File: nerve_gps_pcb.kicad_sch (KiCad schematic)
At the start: 14 parts, among them J1 2x8, J2 WS2812B, J3 5V GPIO Breakout, U1 SAM-M10Q, U2 TXB0104QPWRQ1

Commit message: Fix board-to-board connector pinout
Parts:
- removed J1: 2x8, Connector_PinHeader_1.27mm:PinHeader_2x08_P1.27mm_Vertical_SMD, symbol Connector_Generic:Conn_02x08_Counter_Clockwise
- added J1: 2x8, Connector_PinHeader_1.27mm:PinHeader_2x08_P1.27mm_Vertical_SMD, symbol Connector_Generic:Conn_02x08_Odd_Even
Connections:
- net +3.3VBATT: now also J1.14 (Pin_14)
- net +3V3: now also J1.3 (Pin_3), J1.4 (Pin_4)
- net +5V: now also J1.1 (Pin_1), J1.2 (Pin_2)
- net GND: now also J1.10 (Pin_10), J1.11 (Pin_11)
- net GPIO_1: now also J1.5 (Pin_5)
- net GPIO_2: now also J1.7 (Pin_7)
- net GPIO_3: now also J1.9 (Pin_9)
- net GPS_NRST: now also J1.12 (Pin_12)
- net GPS_UART_RX: now also J1.8 (Pin_8)
- net GPS_UART_TX: now also J1.6 (Pin_6)
- net LED_PWM: now also J1.13 (Pin_13)
- new net: J1.15 (Pin_15), J1.16 (Pin_16)

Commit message: Pass DRC (ERC previously passed)
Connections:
- net GPIO_1: now also J1.9 (Pin_9); no longer J1.5 (Pin_5)
- net GPIO_3: now also J1.5 (Pin_5); no longer J1.9 (Pin_9)
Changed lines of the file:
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@@
+		)
+	)
+	(hierarchical_label "GPIO_2"
+		(shape input)
+		(at 38.1 33.02 180)
+		(fields_autoplaced yes)
+		(effects
+			(font
+				(size 1.27 1.27)
+			)
+			(justify right)
 		)
 	)
@@
 		)
 	)
-	(hierarchical_label "GPIO_2"
+	(hierarchical_label "GPIO_1"
 		(shape input)
-		(at 38.1 33.02 180)
+		(at 38.1 35.56 180)
 		(fields_autoplaced yes)
 		(effects
@@
 		)
 	)
-	(hierarchical_label "GPIO_1"
+	(hierarchical_label "GPIO_2"
 		(shape input)
-		(at 38.1 30.48 180)
+		(at 34.29 99.06 180)
 		(fields_autoplaced yes)
 		(effects
@@
 		)
 	)
-	(hierarchical_label "GPIO_2"
+	(hierarchical_label "GPIO_3"
 		(shape input)
-		(at 34.29 99.06 180)
+		(at 38.1 30.48 180)
 		(fields_autoplaced yes)
 		(effects
@@
 		(fields_autoplaced yes)
 		(effects
-			(font
-				(size 1.27 1.27)
-			)
-			(justify right)
-		)
-	)
-	(hierarchical_label "GPIO_3"
-		(shape input)
-		(at 38.1 35.56 180)
-		(fields_autoplaced yes)
-		(effects

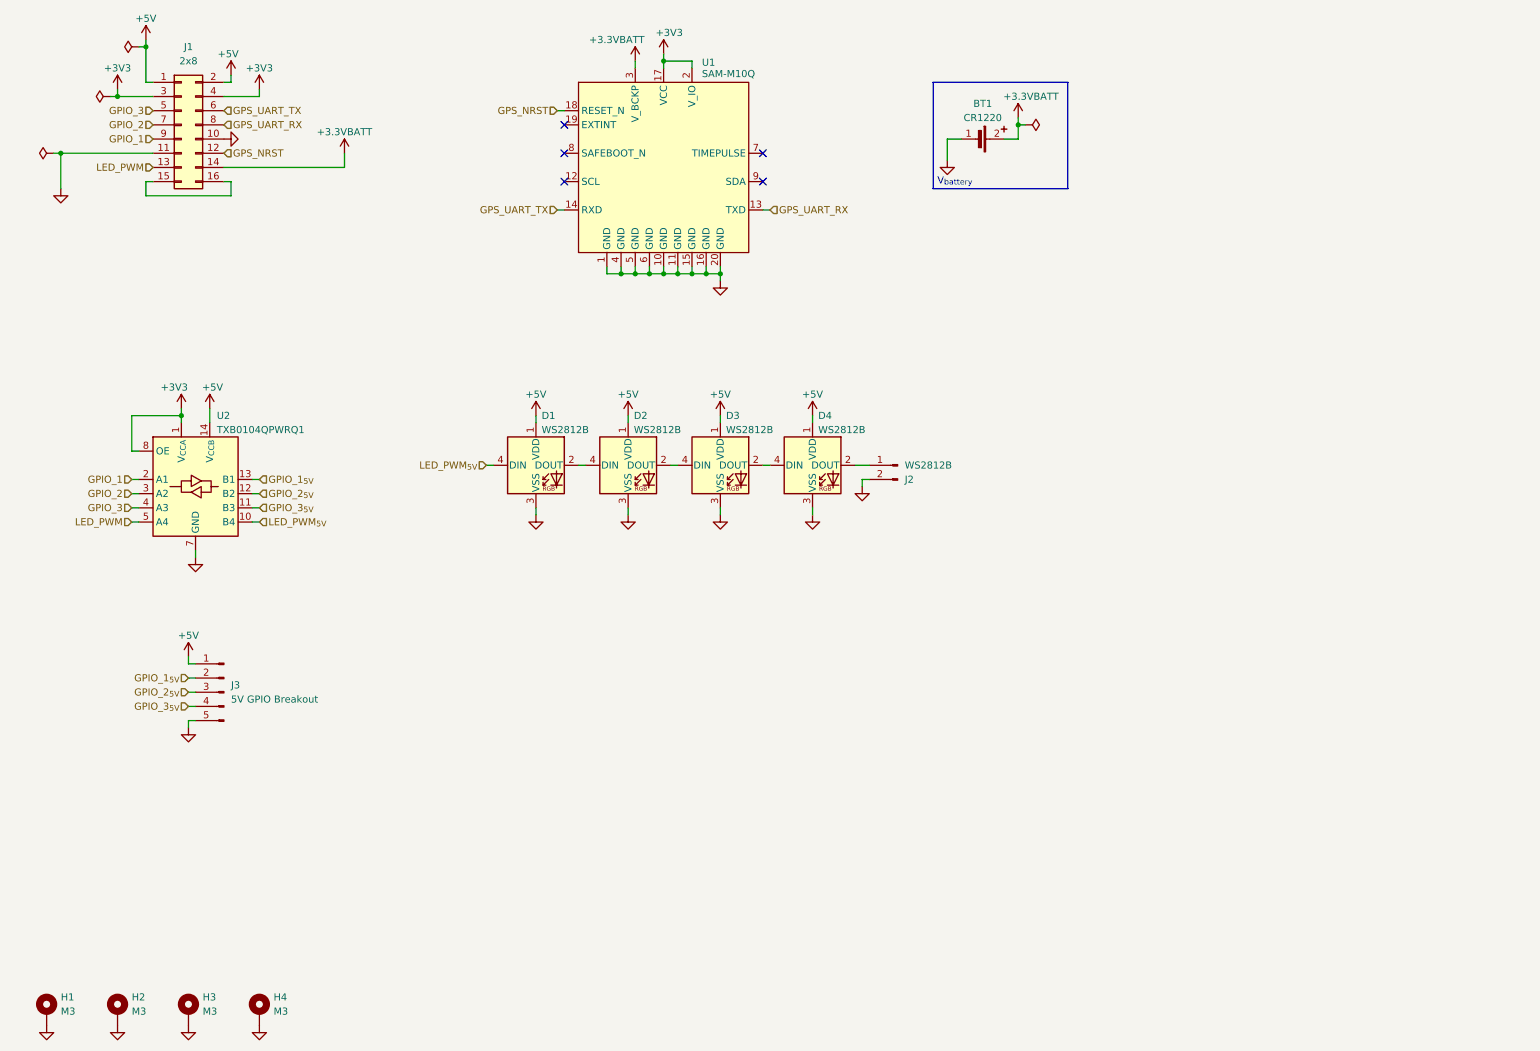
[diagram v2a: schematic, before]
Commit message: Cleanup and update board-to-board connector
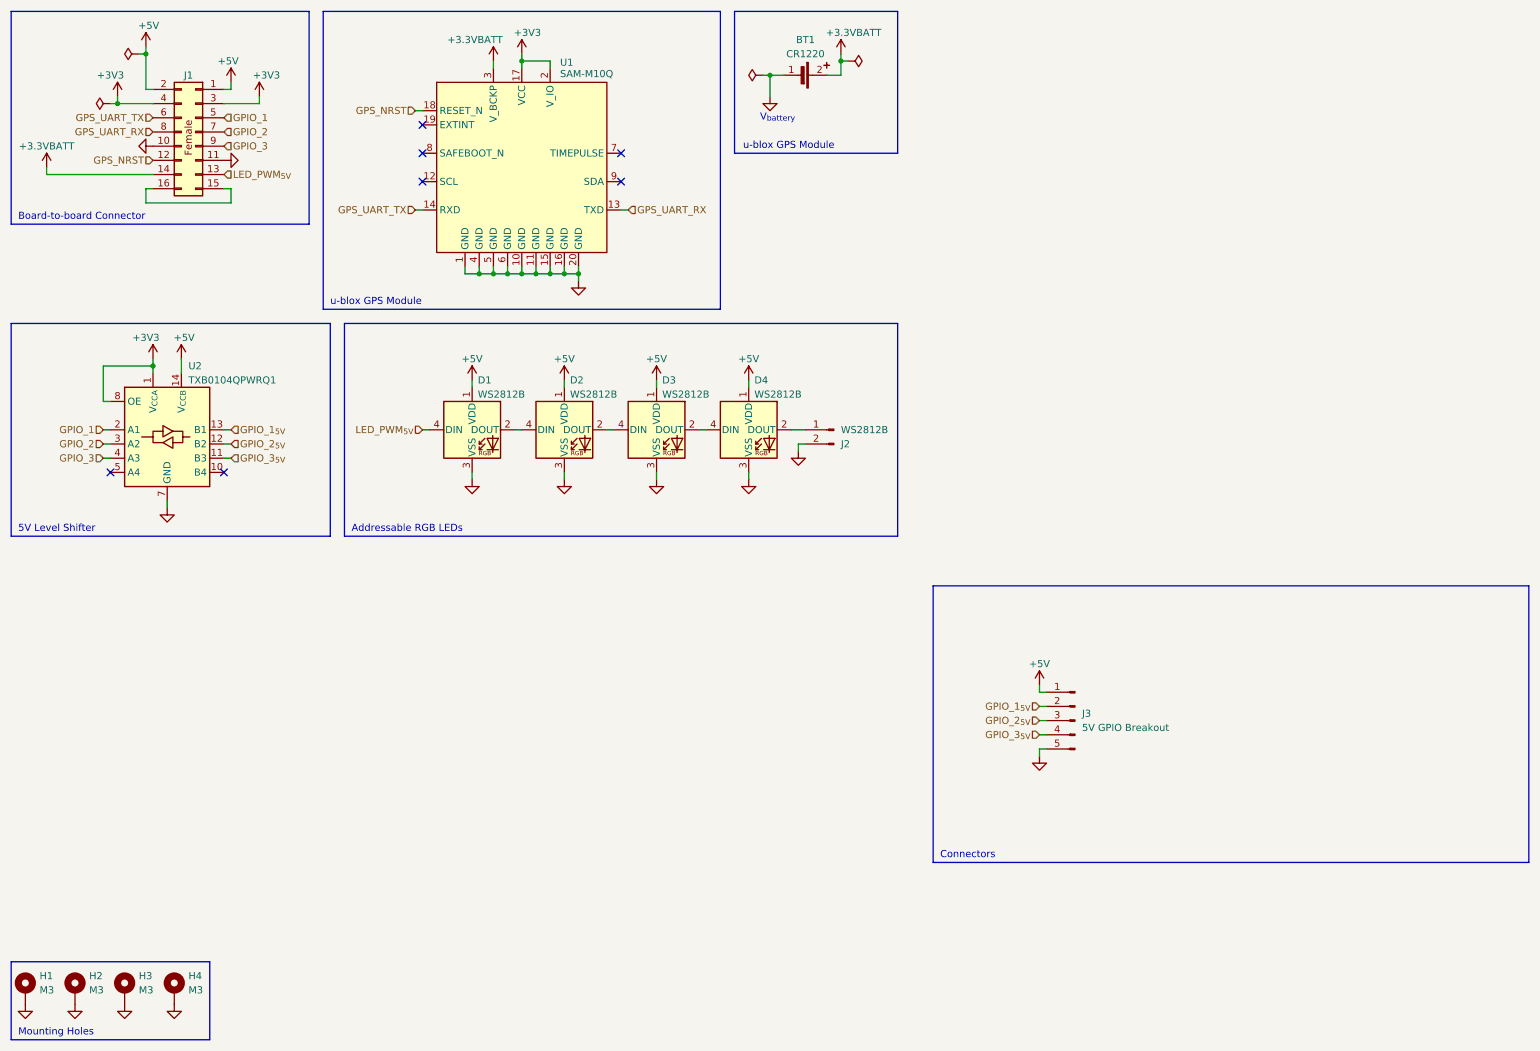
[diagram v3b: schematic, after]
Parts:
- removed J1: 2x8, Connector_PinHeader_1.27mm:PinHeader_2x08_P1.27mm_Vertical_SMD, symbol Connector_Generic:Conn_02x08_Odd_Even
- added J1: BF080-16-A-1-L-C, connectors:bf080-16-a-1-l-c, symbol connectors:bf080-16-a-1-l-c
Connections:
- net +3.3VBATT: now also J1.14
- net +3V3: now also J1.3, J1.4
- net +5V: now also J1.1, J1.2
- net GND: now also J1.10, J1.11
- net GPIO_1: now also J1.5
- net GPIO_2: now also J1.7
- net GPIO_3: now also J1.9
- net GPS_NRST: now also J1.12
- net GPS_UART_RX: now also J1.8
- net GPS_UART_TX: now also J1.6
- net LED_PWM_{5V}: now also J1.13; no longer U2.10 (B4)
- net LED_PWM: no longer names the net of U2.5 (A4)
- new net: J1.15, J1.16
- no-connect marks 5 -> 7
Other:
- note added: "5V Level Shifter"
- note added: "Addressable RGB LEDs"
- note added: "Board-to-board Connector"
- note added: "Connectors"
- note added: "Mounting Holes"
- note added: "u-blox GPS Module"
- moved on the sheet: BT1, D1, D2, D3, D4, J2, J3, U1, U2

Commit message: Update config.kibot.yaml, cleanup, add fiducials
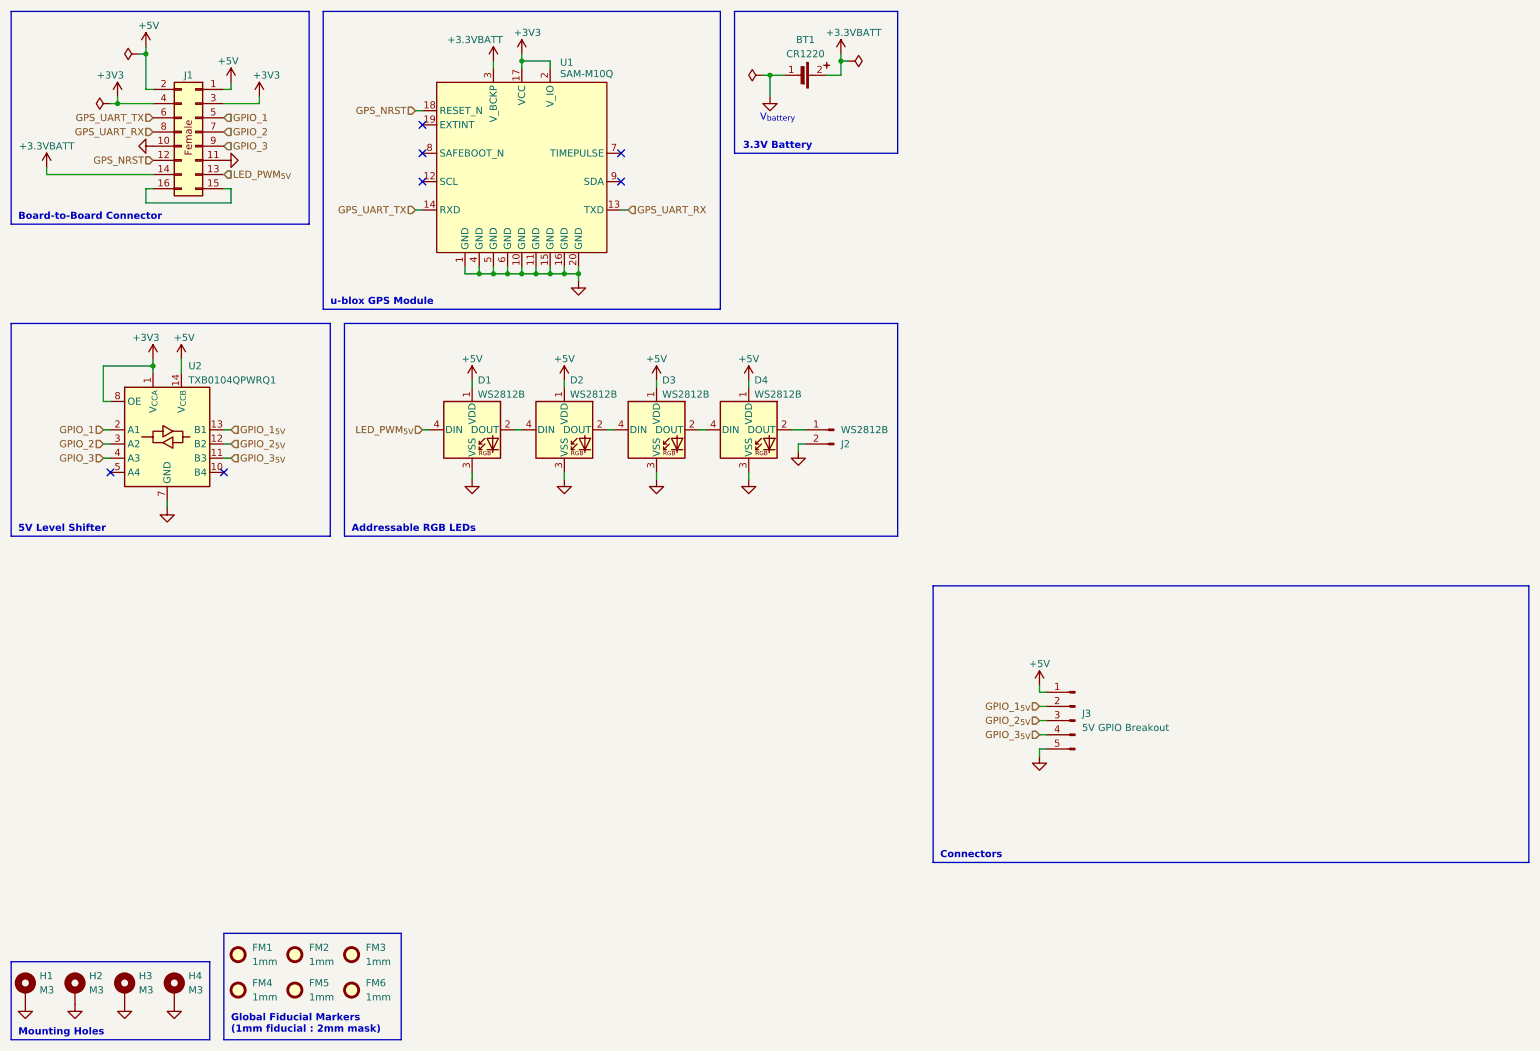
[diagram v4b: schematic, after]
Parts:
- added FM1, FM2, FM3, FM4, FM5, FM6: 1mm, Fiducial:Fiducial_1mm_Mask2mm, symbol Mechanical:Fiducial
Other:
- note added: "3.3V Battery"
- note added: "Board-to-Board Connector"
- note added: "Global Fiducial Markers (1mm fiducial : 2mm mask)"
- note removed: "Board-to-board Connector"

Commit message: Major cleanup and update component_library
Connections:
- net +3.3VBATT renamed +3VBATT
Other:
- note added: "3V Battery"
- note removed: "3.3V Battery"
- note removed: "V_{battery}"
- moved on the sheet: BT1
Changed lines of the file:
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@@
 	)
 	(junction
-		(at 36.83 20.32)
+		(at 151.13 29.21)
 		(diameter 0)
 		(color 0 0 0 0)
 	)
 	(junction
-		(at 148.59 24.13)
+		(at 163.83 22.86)
+		(diameter 0)
+		(color 0 0 0 0)
+	)
+	(junction
+		(at 36.83 20.32)
 		(diameter 0)
 		(color 0 0 0 0)
@@
 	)
 	(junction
-		(at 161.29 21.59)
-		(diameter 0)
-		(color 0 0 0 0)
-	)
-	(junction
 		(at 111.76 59.69)
 		(diameter 0)
@@
 	(wire
 		(pts
-			(xy 148.59 24.13) (xy 151.13 24.13)
+			(xy 151.13 26.67) (xy 153.67 26.67)
 		)
 		(stroke
@@
 	(wire
 		(pts
-			(xy 158.75 24.13) (xy 161.29 24.13)
+			(xy 161.29 26.67) (xy 163.83 26.67)
+		)
+		(stroke
+			(width 0)
+			(type default)
+		)
+	)
+	(wire
+		(pts
+			(xy 163.83 22.86) (xy 163.83 26.67)
 		)
 		(stroke
@@
 	(wire
 		(pts
-			(xy 161.29 21.59) (xy 161.29 24.13)
+			(xy 163.83 21.59) (xy 163.83 22.86)
 		)
 		(stroke
@@
 	(wire
 		(pts
-			(xy 147.32 24.13) (xy 148.59 24.13)
+			(xy 31.75 29.21) (xy 38.1 29.21)
 		)
 		(stroke
@@
 	(wire
 		(pts
-			(xy 31.75 29.21) (xy 38.1 29.21)
+			(xy 104.14 58.42) (xy 104.14 59.69)
 		)
 		(stroke
@@
 	(wire
 		(pts
-			(xy 104.14 58.42) (xy 104.14 59.69)
+			(xy 151.13 26.67) (xy 151.13 29.21)
 		)
 		(stroke
@@
 	(wire
 		(pts
-			(xy 148.59 24.13) (xy 148.59 27.94)
+			(xy 57.15 29.21) (xy 50.8 29.21)
 		)
 		(stroke
@@
 	(wire
 		(pts
-			(xy 57.15 29.21) (xy 50.8 29.21)
+			(xy 196.85 137.16) (xy 198.12 137.16)
 		)
 		(stroke
@@
 	(wire
 		(pts
-			(xy 196.85 137.16) (xy 198.12 137.16)
+			(xy 114.3 58.42) (xy 114.3 59.69)
 		)
 		(stroke
@@
 	(wire
 		(pts
-			(xy 114.3 58.42) (xy 114.3 59.69)
+			(xy 109.22 59.69) (xy 106.68 59.69)
 		)
 		(stroke
@@
 	(wire
 		(pts
-			(xy 109.22 59.69) (xy 106.68 59.69)
+			(xy 151.13 29.21) (xy 151.13 30.48)
 		)
 		(stroke
@@
 	(wire
 		(pts
+			(xy 149.86 29.21) (xy 151.13 29.21)
+		)
+		(stroke
+			(width 0)
+			(type default)
+		)
+	)
+	(wire
+		(pts
 			(xy 93.98 59.69) (xy 96.52 59.69)
 		)
@@
 	(wire
 		(pts
-			(xy 161.29 21.59) (xy 162.56 21.59)
+			(xy 163.83 22.86) (xy 165.1 22.86)
 		)
 		(stroke
@@
 		)
 	)
-	(wire
-		(pts
-			(xy 161.29 20.32) (xy 161.29 21.59)
-		)
-		(stroke
-			(width 0)
-			(type default)
-		)
-	)
 	(rectangle
 		(start 12.7 12.7)
@@
 		)
 	)
-	(text "3.3V Battery"
+	(text "3V Battery"
 		(exclude_from_sim no)
 		(at 143.764 36.068 0)
@@
 		)
 	)
-	(text "V_{battery}"
-		(exclude_from_sim no)
-		(at 146.812 30.988 0)
-		(effects
-			(font
-				(size 1.27 1.27)
-			)
-			(justify left top)
-		)
-	)
 	(text "Board-to-Board Connector"
 		(exclude_from_sim no)
@@
 	(symbol
 		(lib_id "power:PWR_FLAG")
-		(at 147.32 24.13 90)
+		(at 149.86 29.21 90)
+		(mirror x)
 		(unit 1)
 		(exclude_from_sim no)
@@
 		(on_board yes)
 		(dnp no)
-		(fields_autoplaced yes)
 		(property "Reference" "#FLG04"
-			(at 145.415 24.13 0)
+			(at 147.955 29.21 0)
 			(effects
 				(font
@@
 		)
 		(property "Value" "PWR_FLAG"
-			(at 142.24 24.13 0)
+			(at 144.78 29.21 0)
 			(effects
 				(font
@@
 		)
 		(property "Footprint" ""
-			(at 147.32 24.13 0)
+			(at 149.86 29.21 0)
 			(effects
 				(font
@@
 		)
 		(property "Datasheet" "~"
-			(at 147.32 24.13 0)
+			(at 149.86 29.21 0)
 			(effects
 				(font
@@
 		)
 		(property "Description" "Special symbol for telling ERC where power comes from"
-			(at 147.32 24.13 0)
+			(at 149.86 29.21 0)
 			(effects
 				(font
@@
 	(symbol
 		(lib_id "common:harwin_s8411-45r_cr1220_battery")
-		(at 154.94 24.13 0)
+		(at 157.48 26.67 0)
 		(unit 1)
 		(exclude_from_sim no)
@@
 		(dnp no)
 		(property "Reference" "BT1"
-			(at 154.94 17.78 0)
+			(at 157.48 20.32 0)
 			(effects
 				(font
@@
 		)
 		(property "Value" "CR1220"
-			(at 154.94 20.32 0)
+			(at 157.48 22.86 0)
 			(effects
 				(font
@@
 		)
 		(property "Footprint" "common:harwin_s8411-45r_cr1220_battery"
-			(at 158.75 26.67 0)
+			(at 161.29 29.21 0)
 			(effects
 				(font
@@
 		)
 		(property "Datasheet" "https://www.harwin.com/products/S8411-45R"
-			(at 190.5 31.623 0)
+			(at 193.04 34.163 0)
 			(effects
 				(font
@@
 		)
 		(property "Description" "Battery Holder (Open) Coin, 12.0mm 1 Cell SMD (SMT) Tab"
-			(at 190.5 27.813 0)
+			(at 193.04 30.353 0)
 			(effects
 				(font
@@
 		)
 		(property "Manufacturer" "Harwin"
-			(at 190.5 22.733 0)
+			(at 193.04 25.273 0)
 			(effects
 				(font
@@
 		)
 		(property "Manufacturer Part Number" "S8411-45R"
-			(at 190.5 22.733 0)
+			(at 193.04 25.273 0)
 			(effects
 				(font
@@
 		)
 		(property "Distributor" "DigiKey"
-			(at 190.5 22.733 0)
+			(at 193.04 25.273 0)
 			(effects
 				(font
@@
 		)
 		(property "Distributor Part Number" "952-1745-1-ND"
-			(at 190.5 31.623 0)
+			(at 193.04 34.163 0)
 			(effects
 				(font
@@
 		)
 		(property "Distributor Link" "https://www.digikey.ca/en/products/detail/harwin-inc/S8411-45R/3131055?s=N4IgTCBcDaIMoA4AsBGFBaJBWASiAugL5A"
-			(at 190.5 27.813 0)
+			(at 193.04 30.353 0)
 			(effects
 				(font
@@
 	(symbol
 		(lib_id "power:+3V3")
-		(at 161.29 20.32 0)
+		(at 163.83 21.59 0)
 		(unit 1)
 		(exclude_from_sim no)
@@
 		(dnp no)
 		(property "Reference" "#PWR03"
-			(at 161.29 24.13 0)
+			(at 163.83 25.4 0)
 			(effects
 				(font
@@
 			)
 		)
-		(property "Value" "+3.3VBATT"
-			(at 163.576 16.51 0)
+		(property "Value" "+3VBATT"
+			(at 163.83 17.78 0)
 			(effects
 				(font
@@
 		)
 		(property "Footprint" ""
-			(at 161.29 20.32 0)
+			(at 163.83 21.59 0)
 			(effects
 				(font
@@
 		)
 		(property "Datasheet" ""
-			(at 161.29 20.32 0)
+			(at 163.83 21.59 0)
 			(effects
 				(font
@@
 		)
 		(property "Description" "Power symbol creates a global label with name \"+3V3\""
-			(at 161.29 20.32 0)
+			(at 163.83 21.59 0)
 			(effects
 				(font
@@
 			)
 		)
-		(property "Value" "+3.3VBATT"
-			(at 95.758 17.78 0)
+		(property "Value" "+3VBATT"
+			(at 96.52 17.78 0)
 			(effects
 				(font
@@
 			)
 		)
-		(property "Value" "+3.3VBATT"
+		(property "Value" "+3VBATT"
 			(at 19.05 36.83 0)
 			(effects
@@
 	(symbol
 		(lib_id "power:GND")
-		(at 148.59 27.94 0)
+		(at 151.13 30.48 0)
 		(unit 1)
 		(exclude_from_sim no)
@@
 		(fields_autoplaced yes)
 		(property "Reference" "#PWR08"
-			(at 148.59 34.29 0)
+			(at 151.13 36.83 0)
 			(effects
 				(font
@@
 		)
 		(property "Value" "GND"
-			(at 148.59 33.02 0)
+			(at 151.13 35.56 0)
 			(effects
 				(font
@@
 		)
 		(property "Footprint" ""
-			(at 148.59 27.94 0)
+			(at 151.13 30.48 0)
 			(effects
 				(font
@@
 		)
 		(property "Datasheet" ""
-			(at 148.59 27.94 0)
+			(at 151.13 30.48 0)
 			(effects
 				(font
@@
 		)
 		(property "Description" "Power symbol creates a global label with name \"GND\" , ground"
-			(at 148.59 27.94 0)
+			(at 151.13 30.48 0)
 			(effects
 				(font
@@
 	(symbol
 		(lib_id "power:PWR_FLAG")
-		(at 162.56 21.59 270)
+		(at 165.1 22.86 270)
 		(unit 1)
 		(exclude_from_sim no)
@@
 		(fields_autoplaced yes)
 		(property "Reference" "#FLG02"
-			(at 164.465 21.59 0)
+			(at 167.005 22.86 0)
 			(effects
 				(font
@@
 		)
 		(property "Value" "PWR_FLAG"
-			(at 167.64 21.59 0)
+			(at 170.18 22.86 0)
 			(effects
 				(font
@@
 		)
 		(property "Footprint" ""
-			(at 162.56 21.59 0)
+			(at 165.1 22.86 0)
 			(effects
 				(font
@@
 		)
 		(property "Datasheet" "~"
-			(at 162.56 21.59 0)
+			(at 165.1 22.86 0)
 			(effects
 				(font
@@
 		)
 		(property "Description" "Special symbol for telling ERC where power comes from"
-			(at 162.56 21.59 0)
+			(at 165.1 22.86 0)
 			(effects
 				(font
